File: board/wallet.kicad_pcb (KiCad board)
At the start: 4 copper layers, 48 x 85 mm, 111 parts, among them J1 TYPE-C-31-M-12, U1 BQ25185DLHR, U11 E73-2G4M08S1C, U12 ME6211C28M5G-N, U13 TPS60230RGTR, U14 TLV70313DBVR, U15 MAX17048G+T10, U16 SLS32AIA010MK, U2 TPS63802DLAR, U4 STM32U585VIT6Q, U5 SE050E2HQ1/Z01Z3Z, U6 TS3USB221ARSER, U7 SN74LVC1G02DBVR(UMW), U8 TPS22917DBVR, U9 TXU0202DCUR

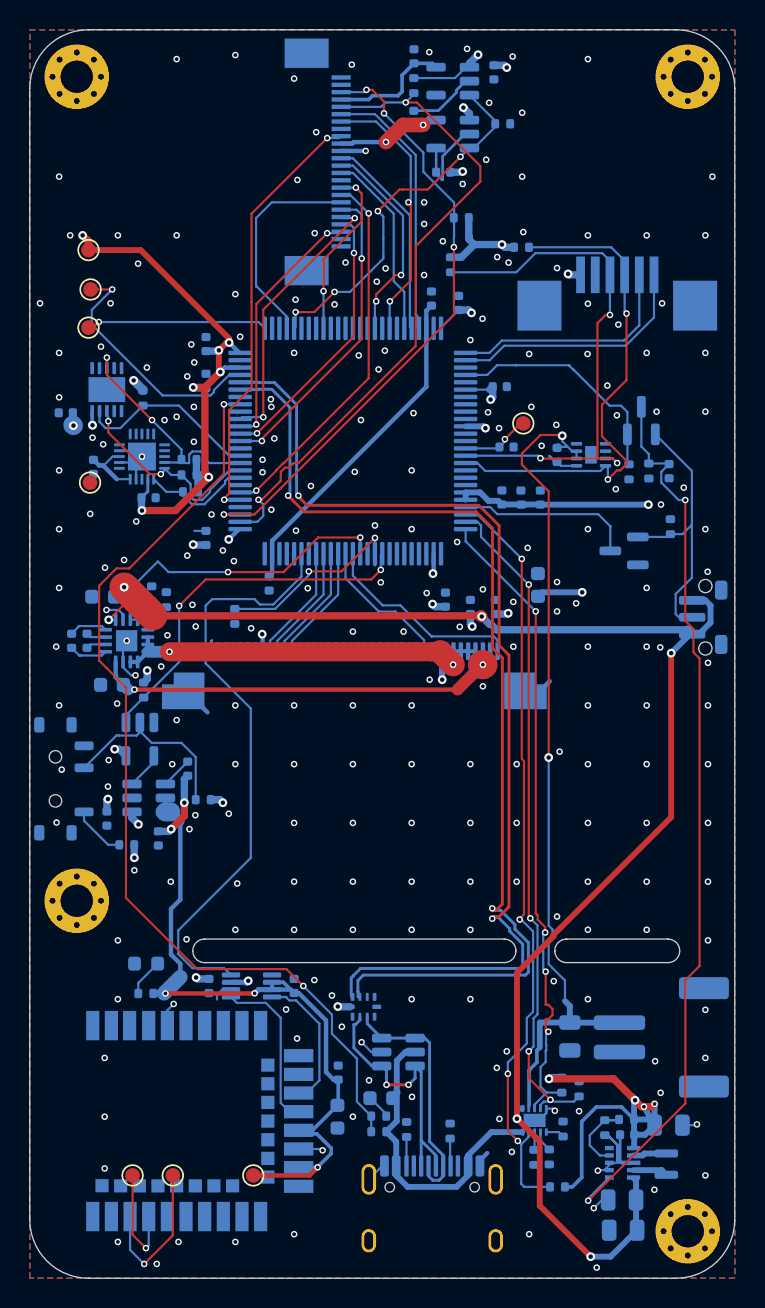
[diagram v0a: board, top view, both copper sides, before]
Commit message: Redundant copper merged away; return and stitching vias for the new routing
humanRouter --stitch-only (working tree on 2f214cb with the peer's uncommitted
--tidy and free-via work; verified here, not trusted):
- tidy: 53 segments lying fully on an equal-or-wider segment of their net, 65
  tracks entirely inside a pad of their net, 21 collinear splits merged. 1108 ->
  969 track records; per net and layer the copper (tracks + pads) is identical
  (0.0 mm^2 symmetric difference).
- 6 GND return vias beside signal vias that had none within reach, 13
  stitching vias on pour the new routing changed; all free vias (KiCad will not
  re-net them).
DRC 0 violations, 3 unconnected (RADIO_TXD, AIRGAP x2); cleanCopper --check
clean; no GND pad-to-via ties beyond the 9 kept; gates pass. UV art rebuilt.

Co-Authored-By: Claude Opus 5.5 <noreply@anthropic.com>
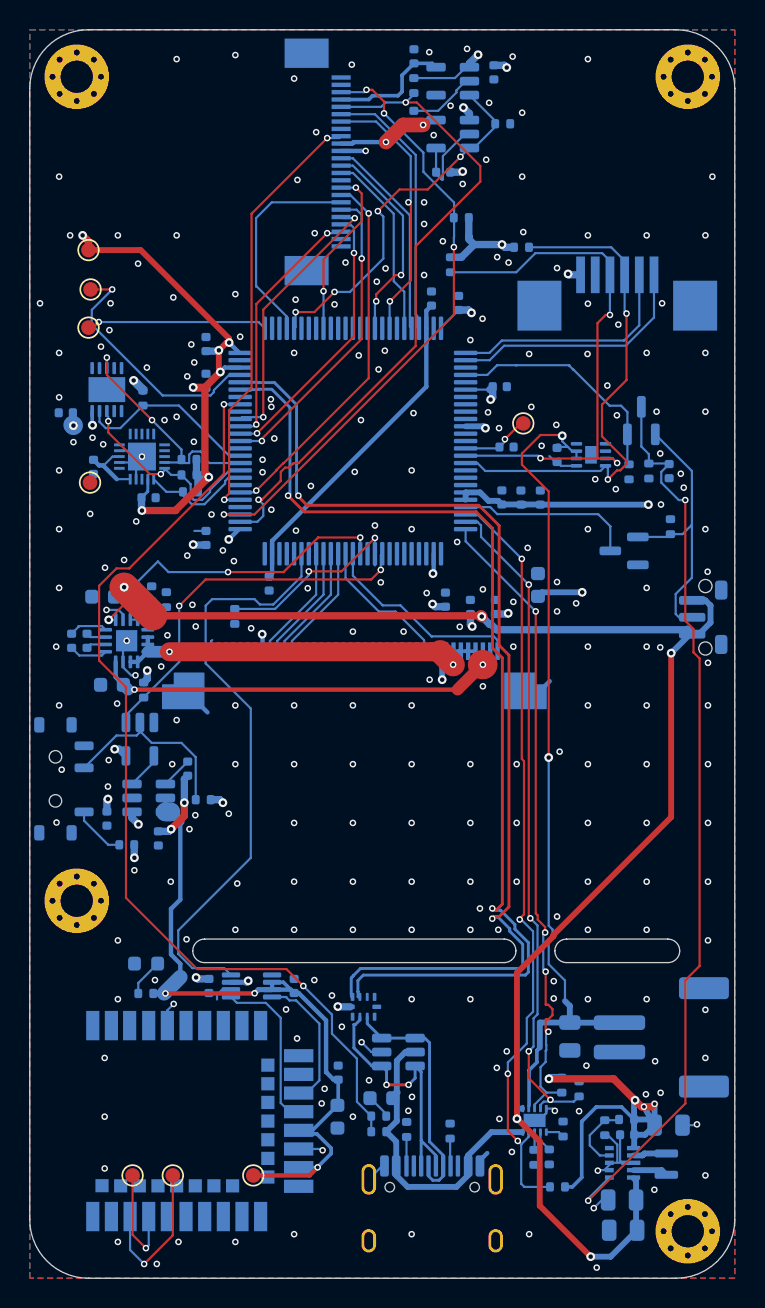
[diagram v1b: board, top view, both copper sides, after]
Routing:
- net GND: track 86.3 -> 45.3 mm, vias 238 -> 257
- net V3V3: track 138.0 -> 134.8 mm
- net RADIO_RX: track 10.2 -> 9.06 mm
- net I2C_SCL: track 37.1 -> 36.1 mm
- net CTP_INT: track 17.0 -> 16.0 mm
- net I2C_SDA: track 34.8 -> 33.8 mm
- net RADIO_3V3: track 49.3 -> 48.4 mm
- net CAM_EN: track 25.3 -> 24.5 mm
- net SYS: track 105.8 -> 105.1 mm
- net FB_3V3: track 5.33 -> 4.68 mm
- net RADIO_TX: track 11.2 -> 10.6 mm
- net AIRGAP: track 13.5 -> 12.9 mm

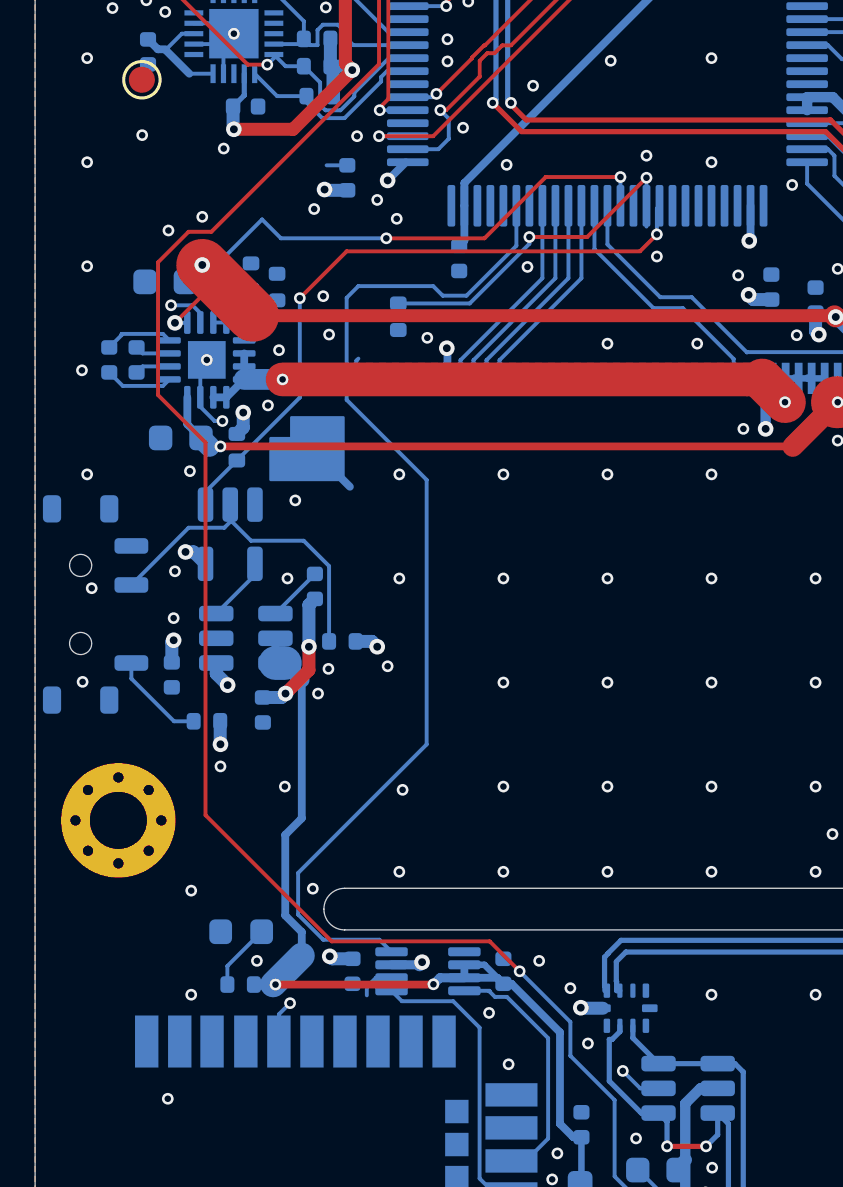
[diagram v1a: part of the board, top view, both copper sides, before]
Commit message: Owner: AIRGAP routed, radio UART and sense lines reworked, TFT_BL and 3.3 V touch-ups
AIRGAP 57 mm (1.36x its shortest tree, 2 vias; the rejected autoroute was 120
mm). RADIO_RXD 39.5 mm (1.36x), VBUS_SENSE 66.7 (1.33x), AIRGAP_SENSE 12.7
(1.33x), RADIO_OFF 24.8 (1.18x), RADIO_3V3 reworked; RADIO_TXD in progress
(an 18 mm gap between its two vias).

As committed: 1 unconnected (RADIO_TXD), its two half-joined vias, J_TFT's
pin-41 tab cut off from the pour (the stub that was its only connection was
removed), starved thermals on C_VDD11A/C_U9B, a 0.002 mm RXD crumb -- fixed in
the next commit.

Co-Authored-By: Claude Opus 5.5 <noreply@anthropic.com>
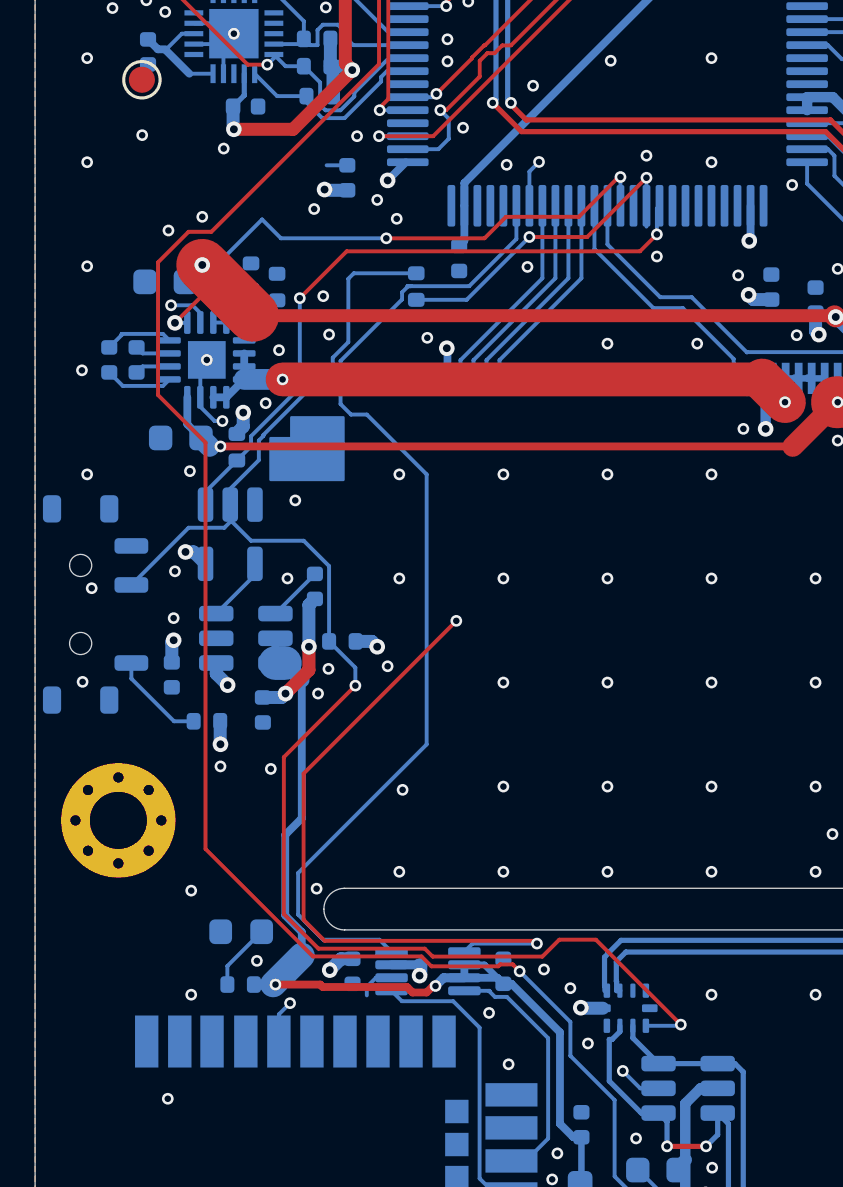
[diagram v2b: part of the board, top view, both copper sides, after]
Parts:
- moved R_AIRS 1.35 mm to (14.7, 38.8), turned to -90 degrees
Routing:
- net AIRGAP: track 12.9 -> 57.1 mm, vias 0 -> 2
- net RADIO_TXD_MCU: track 0.00 -> 28.0 mm, vias 0 -> 3
- net GND: track 45.3 -> 42.5 mm
- net AIRGAP_SENSE: track 13.6 -> 12.7 mm
- net RADIO_RXD_MCU: track 40.4 -> 39.5 mm
- net VBUS_SENSE: track 65.9 -> 66.7 mm

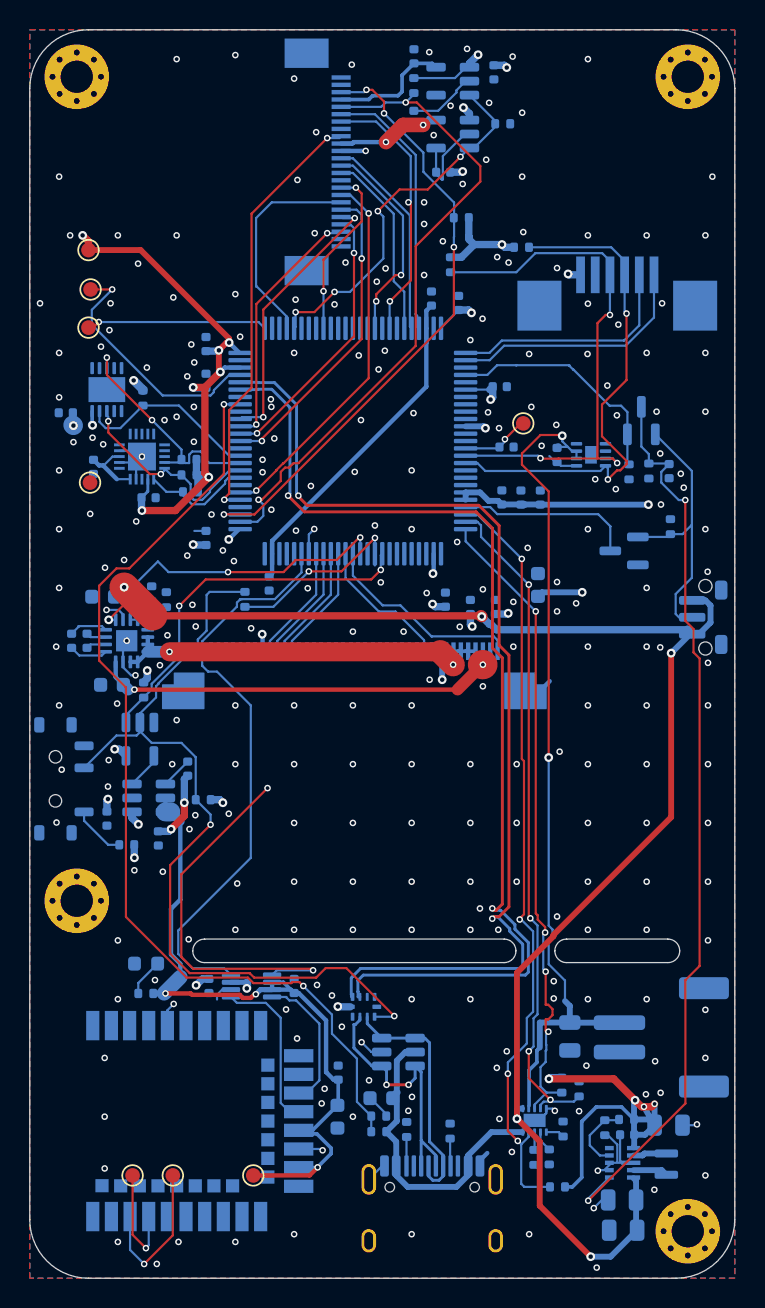
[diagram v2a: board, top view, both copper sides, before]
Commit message: Pour stubs replaced by real pour connections; TFT_BL hump straightened
- J_TFT's mounting tabs (41, 42) are custom pads with a 0.005 mm anchor, so
  KiCad's thermal spokes degenerate and the pour never joins them; the router
  had worked around it with a "track to the pour". The footprint now gives both
  tabs a solid pour connection (zone_connect 2, a text edit: a pcbnew re-save
  rewrote the custom pads), so pin 41 is joined without a stub.
- Every GND track running from one pad into open pour was tested alone against
  KiCad's DRC: 4 redundant ones removed (J_TFT 10 and 42, C_USBSW, C_VDD3);
  3 kept because they are the pad's only connection (U9 pin 2, 0.5 mm pitch)
  or work as its one thermal spoke (R_FB2, C_GAUGE: a solid connection on one
  pad of an 0402 risks tombstoning).
- TFT_BL humped over R_BLEN/R_BLPD around a GND via removed with the ties; now
  one 45-degree step at the via, straight at y 36.6 (room for R_BLPD pin 2's
  top spoke) and a chamfered drop into R_BLEN pin 1.
- C_VDD11A and C_U9B GND pads: solid pour connection (the reroute starved their
  spokes). RXD 0.002 mm crumb removed.
- syncBoard keeps a pad's setting across a swap only when it is an explicit
  override, so a library choice (the tabs' solid connection) wins over
  "inherited".

DRC: only the owner's in-progress RADIO_TXD (1 unconnected, its 2 half-joined
vias). cleanCopper --check clean; gates pass.

Co-Authored-By: Claude Opus 5.5 <noreply@anthropic.com>
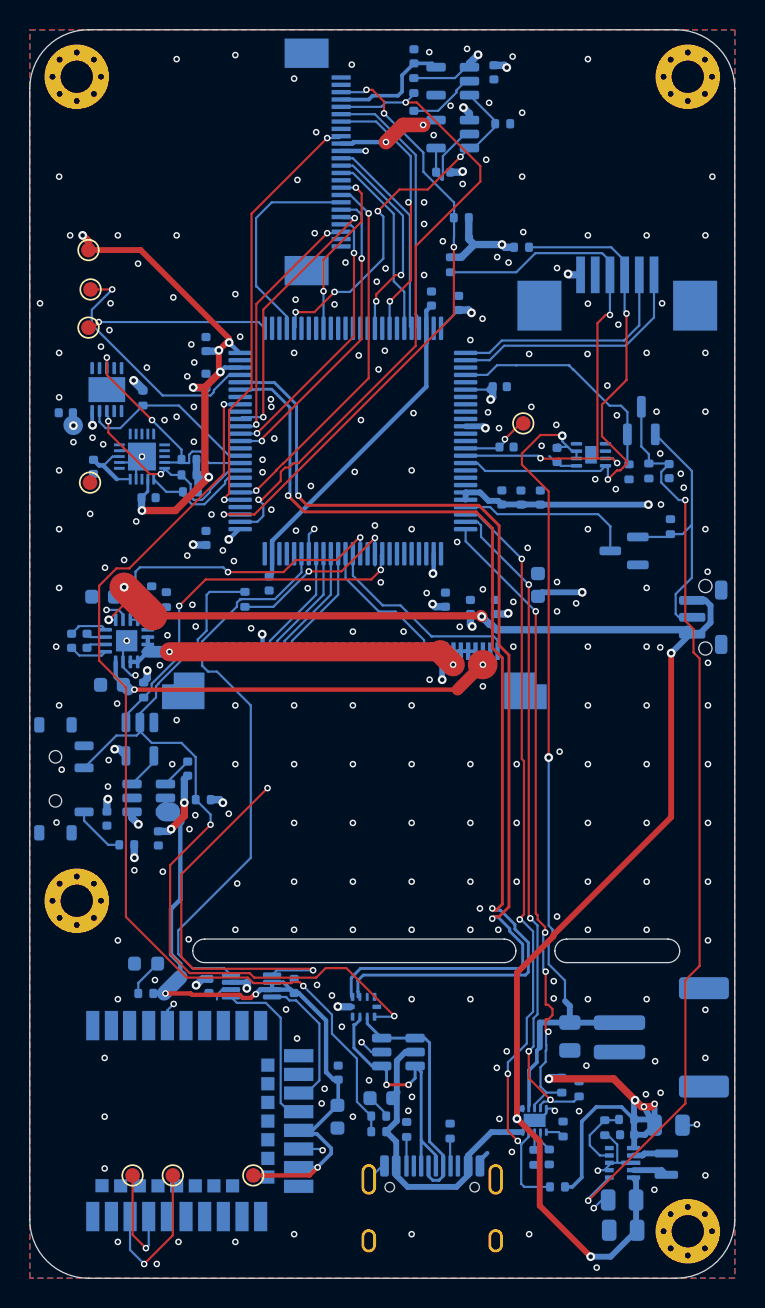
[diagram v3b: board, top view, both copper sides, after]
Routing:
- net GND: track 42.5 -> 38.3 mm

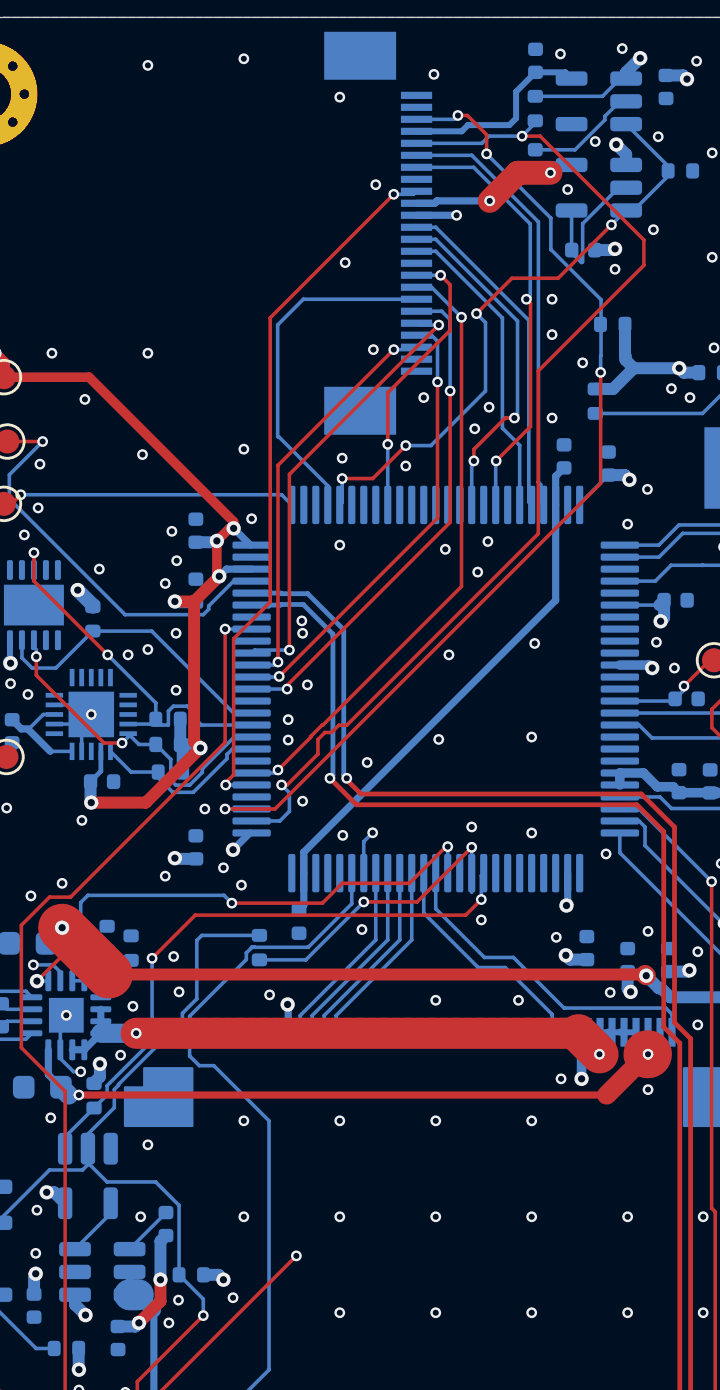
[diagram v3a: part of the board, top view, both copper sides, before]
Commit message: Return vias: 7 GND vias beside signal vias that had none within 2 mm
CAM_EN, CAM_SCL, CAM_SDA, CAM_D5, CAM_DVDD, VBUS_SENSE, RADIO_TXD: free vias
(KiCad will not re-net them), >= 0.5 mm from any pad, inside outer GND pour.
No room within 2 mm for RADIO_3V3, CHG_STAT2, CAM_PCLK, CAM_D3. DRC: only the
open RADIO_TXD (1 unconnected, its 2 half-joined vias).

Co-Authored-By: Claude Opus 5.5 <noreply@anthropic.com>
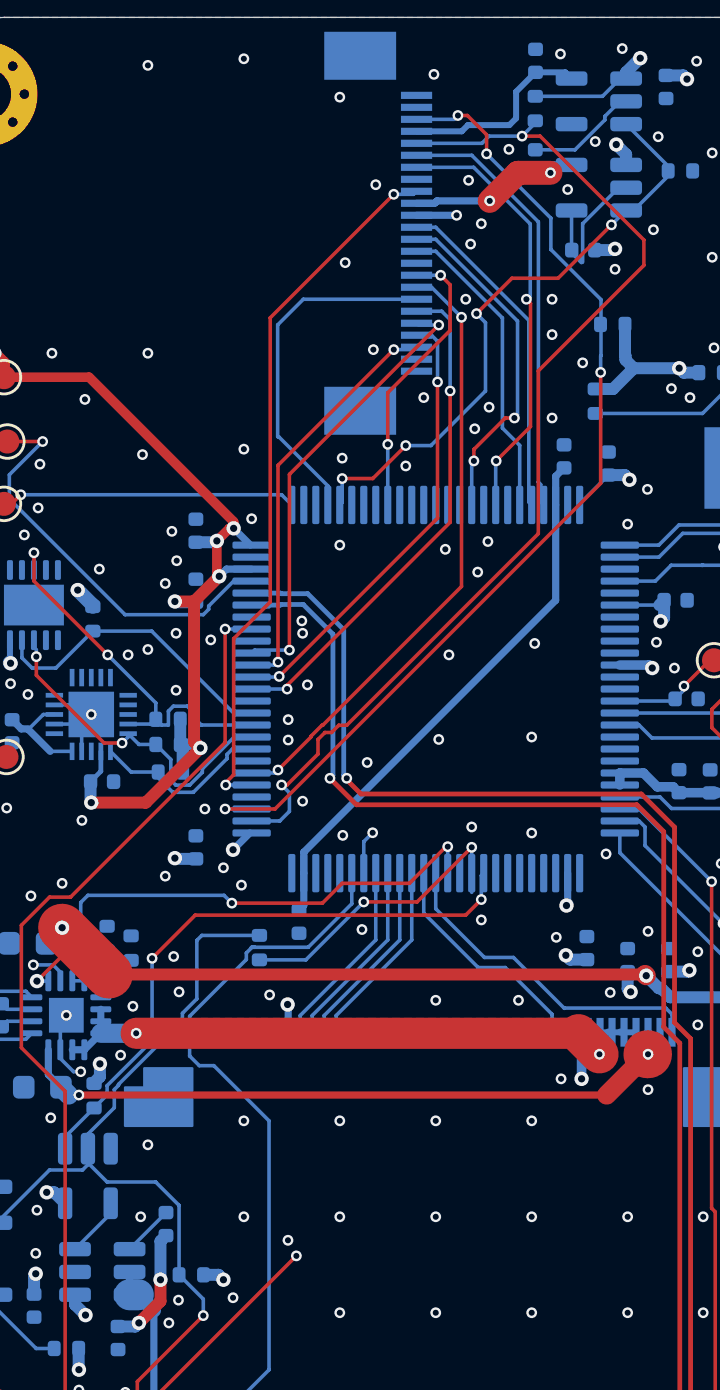
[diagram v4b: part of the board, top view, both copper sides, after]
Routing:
- net GND: vias 257 -> 264
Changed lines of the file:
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@@
+	)
+	(via
+		(at 23.25 11.75)
+		(size 0.45)
+		(drill 0.25)
+		(layers "F.Cu" "B.Cu")
+		(free yes)
+		(net "GND")
 	)
 	(via
@@
 	)
 	(via
+		(at 12.62 25.95)
+		(size 0.45)
+		(drill 0.25)
+		(layers "F.Cu" "B.Cu")
+		(free yes)
+		(net "GND")
+	)
+	(via
 		(at 28.125 14.4)
 		(size 0.45)
@@
 	)
 	(via
+		(at 25.05 5.5)
+		(size 0.45)
+		(drill 0.25)
+		(layers "F.Cu" "B.Cu")
+		(free yes)
+		(net "GND")
+	)
+	(via
 		(at 30 50)
 		(size 0.45)
@@
 	)
 	(via
+		(at 23.9 8.6)
+		(size 0.45)
+		(drill 0.25)
+		(layers "F.Cu" "B.Cu")
+		(free yes)
+		(net "GND")
+	)
+	(via
 		(at 46 14)
 		(size 0.45)
@@
 	)
 	(via
+		(at 15.84 50.98)
+		(size 0.45)
+		(drill 0.25)
+		(layers "F.Cu" "B.Cu")
+		(free yes)
+		(net "GND")
+	)
+	(via
 		(at 38 18.65)
 		(size 0.45)
@@
 		(net "GND")
 	)
+	(via
+		(at 23.454 9.45)
+		(size 0.45)
+		(drill 0.25)
+		(layers "F.Cu" "B.Cu")
+		(free yes)
+		(net "GND")
+	)
+	(via
+		(at 23.37 6.79)
+		(size 0.45)
+		(drill 0.25)
+		(layers "F.Cu" "B.Cu")
+		(free yes)
+		(net "GND")
+	)
